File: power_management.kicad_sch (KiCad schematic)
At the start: 34 parts, among them U1 TPS65185

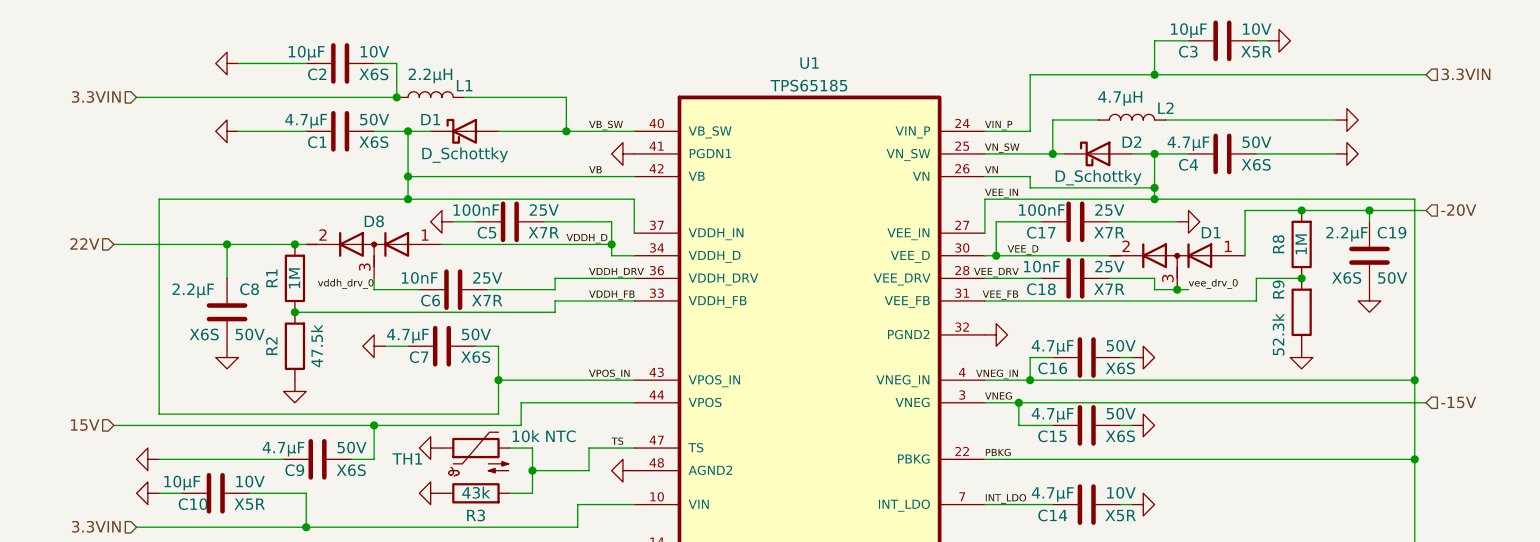
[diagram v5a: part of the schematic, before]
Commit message: Changed VDDH and VEE capacitors to 4.7µF
The evaluation board uses 4.7µF capacitors instead of 2.2µF as stated in
the datasheet.
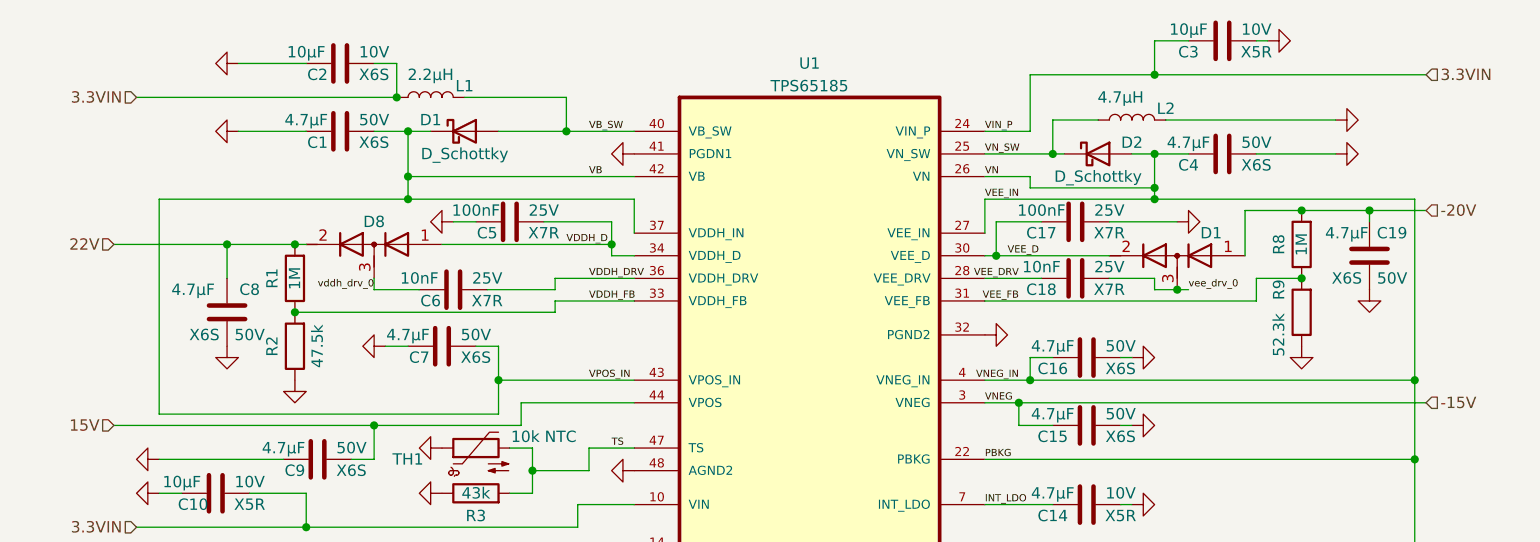
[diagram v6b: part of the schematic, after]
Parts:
- C19, C8: value 2.2µF -> 4.7µF
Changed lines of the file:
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@@
       (effects (font (size 1.27 1.27)))
     )
-    (property "Value" "2.2µF" (at 80.01 67.31 0)
+    (property "Value" "4.7µF" (at 80.01 67.31 0)
       (effects (font (size 1.27 1.27)))
     )
@@
       (effects (font (size 1.27 1.27)))
     )
-    (property "Value" "2.2µF" (at 209.55 60.96 0)
+    (property "Value" "4.7µF" (at 209.55 60.96 0)
       (effects (font (size 1.27 1.27)))
     )

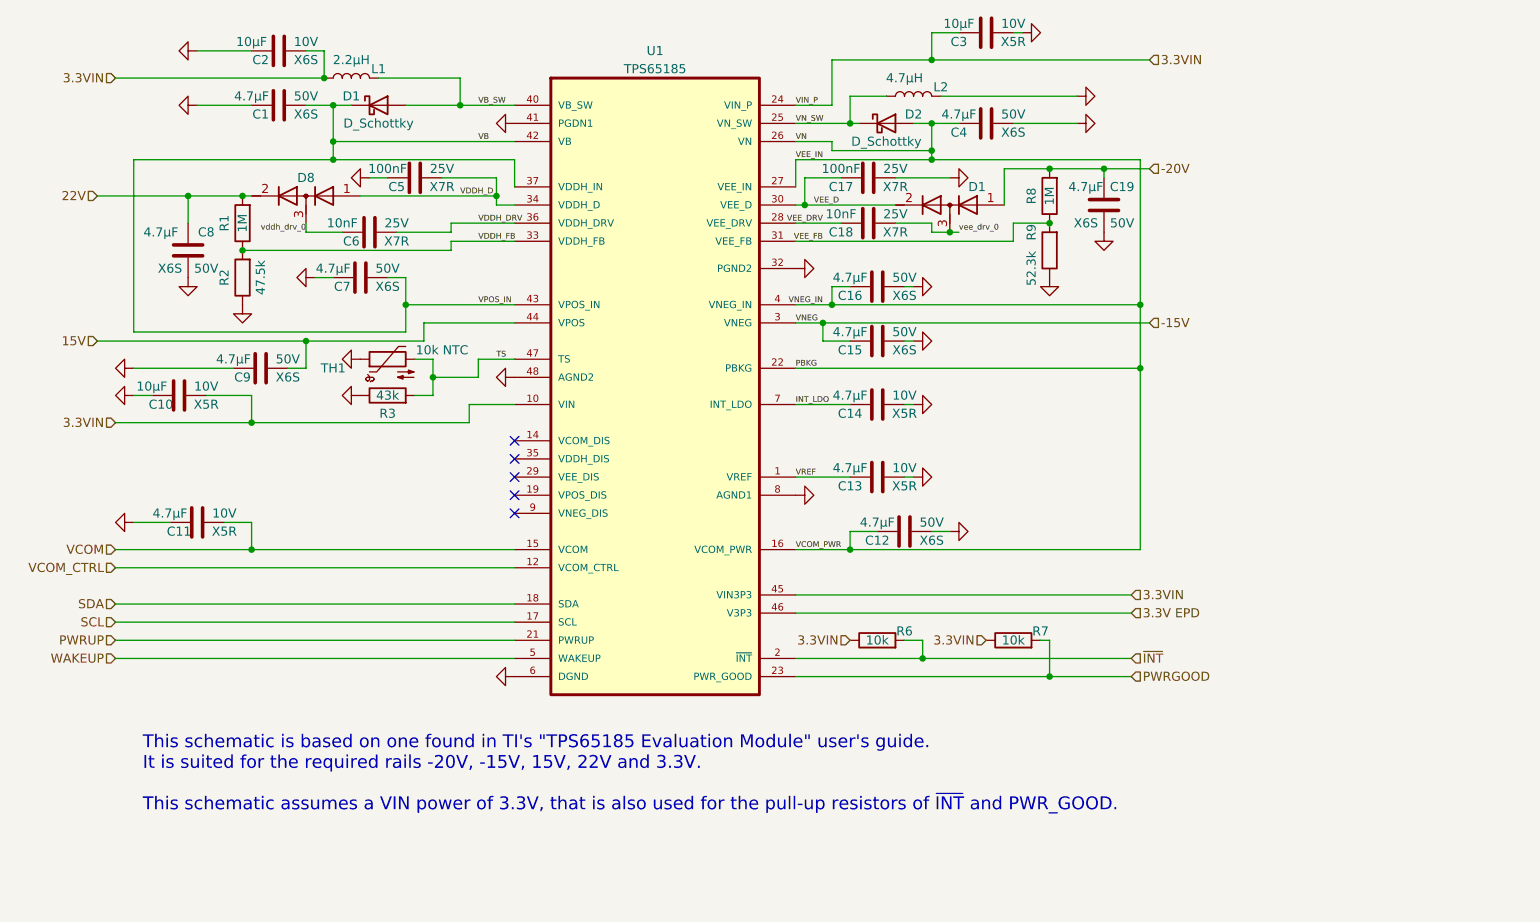
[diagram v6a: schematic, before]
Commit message: Fixed PWR flags in schematic
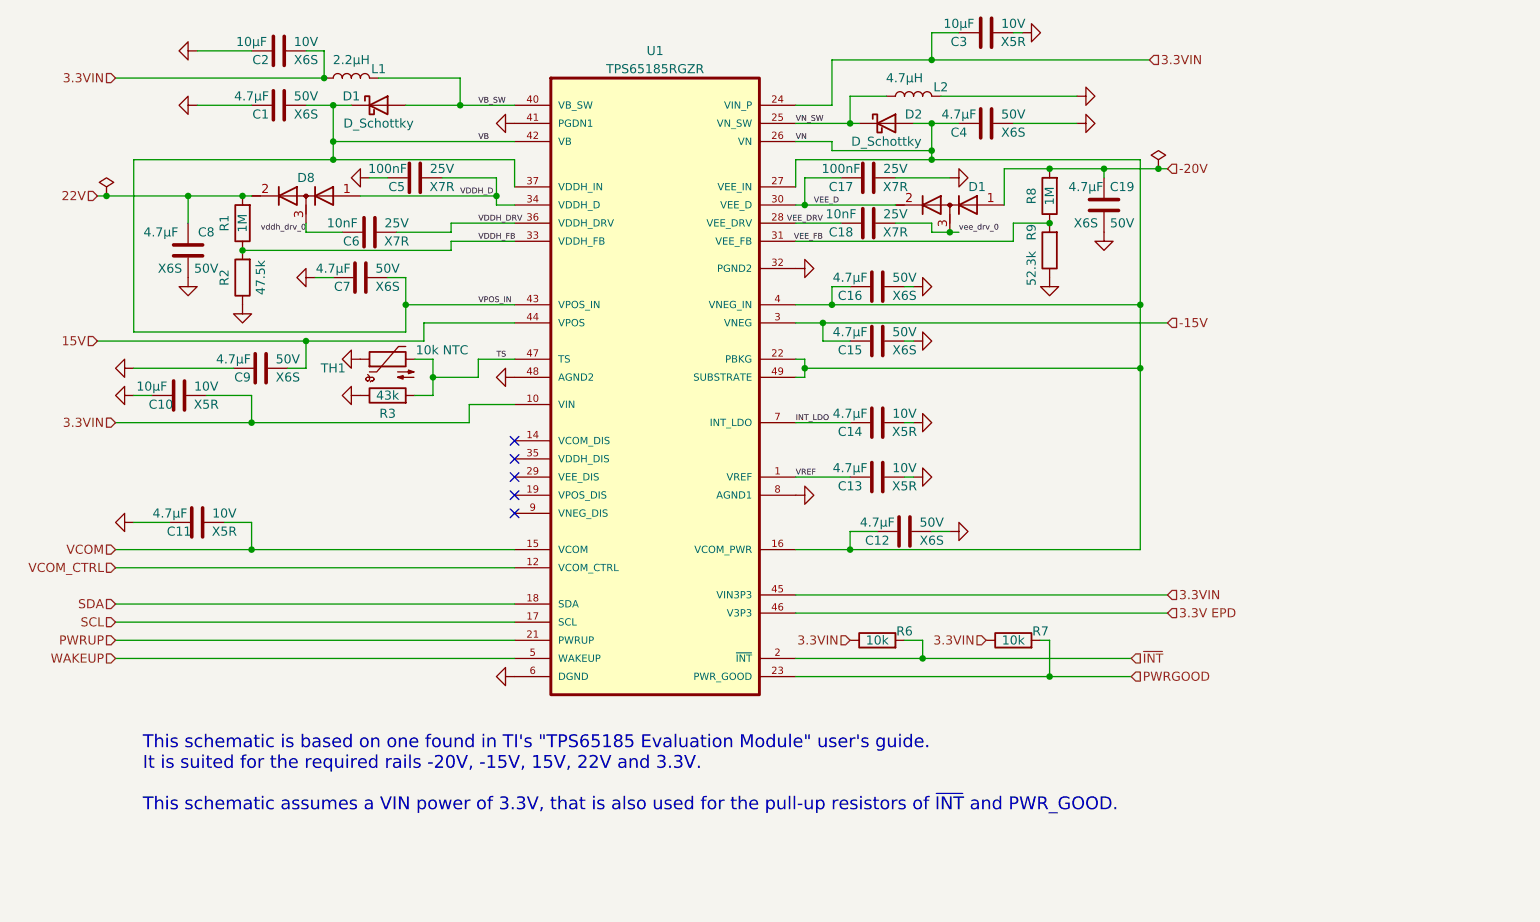
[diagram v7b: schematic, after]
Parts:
- U1: value TPS65185 -> TPS65185RGZR
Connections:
- net PBKG renamed VN
- net VN: now also U1.49 (SUBSTRATE)
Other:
- moved on the sheet: C14

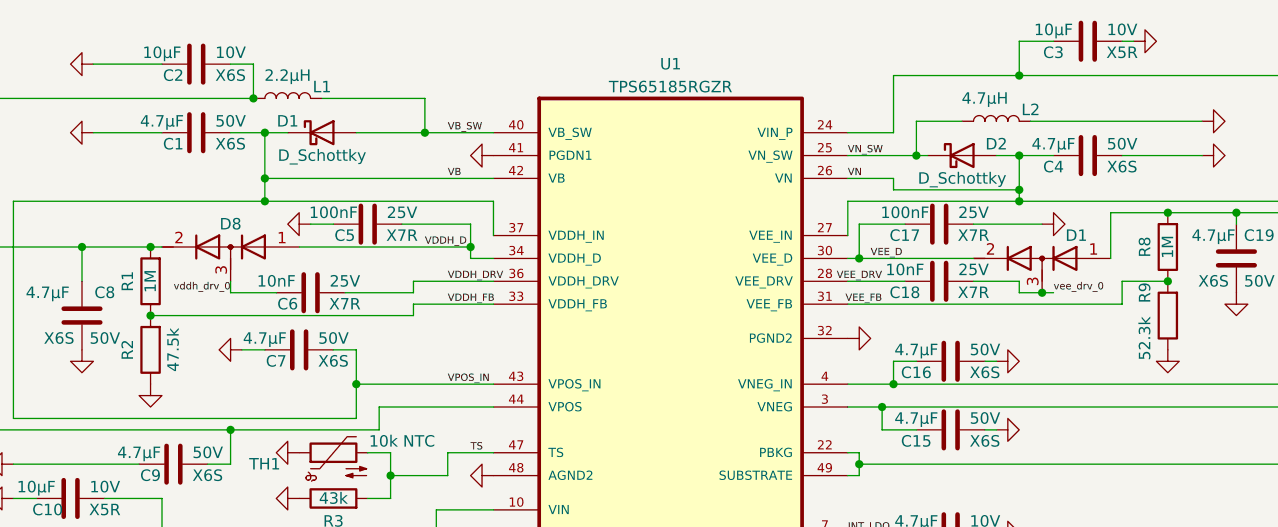
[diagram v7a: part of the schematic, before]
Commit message: Change D footprint for TPS and LCSC part #
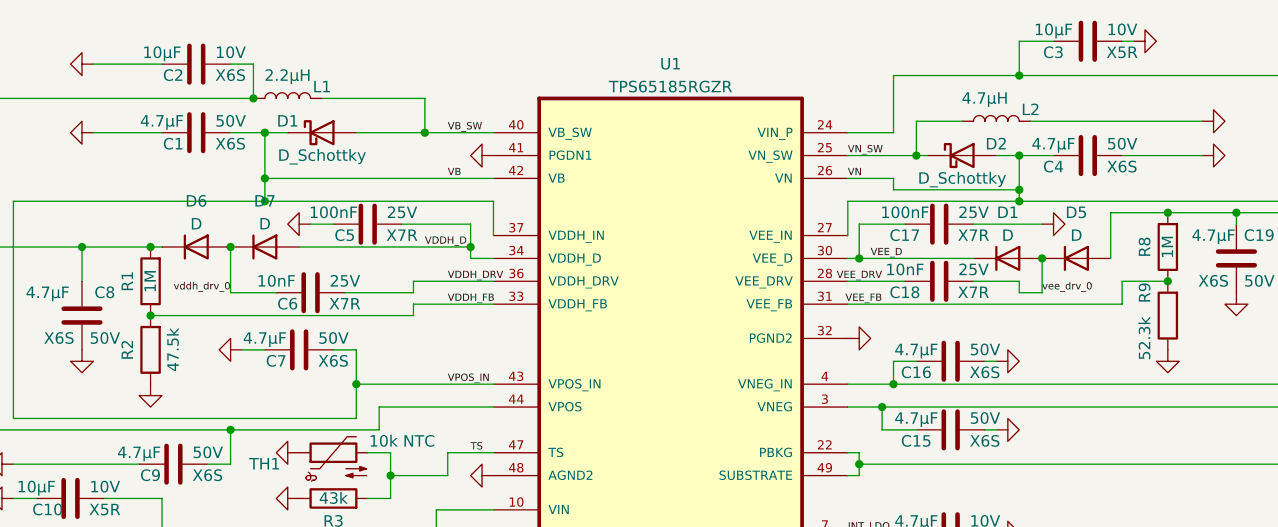
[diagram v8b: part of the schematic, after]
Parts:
- removed D1, D8: D_Dual_Series_AKC, Package_TO_SOT_SMD:SOT-23, symbol Device:D_Dual_Series_AKC
- added D1, D5, D6, D7: D, Diode_SMD:D_SOD-123, symbol Device:D
- C1, C11, C12, C13, C14, C15, C16, C19, C4, C7, C8, C9: LCSC Part # (none) -> C98192
- C10, C2, C3: LCSC Part # (none) -> C85713
- C17, C5: LCSC Part # (none) -> C1591
- C18, C6: LCSC Part # (none) -> C1589
- D1, D2: LCSC Part # (none) -> C82544
- L1: LCSC Part # (none) -> C136232
- L2: LCSC Part # (none) -> C92936
- R1, R8: LCSC Part # (none) -> C105578
- R2: LCSC Part # (none) -> C137715
- R3: LCSC Part # (none) -> C137719
- R6, R7: LCSC Part # (none) -> C98220
- R9: LCSC Part # (none) -> C185323
- TH1: LCSC Part # (none) -> C13564
- U1: LCSC Part # (none) -> C139291
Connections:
- net -20V: now also D5.2 (A)
- net 22V: now also D6.1 (K)
- net VDDH_D: now also D7.2 (A)
- net VEE_D: now also D1.1 (K)
- net vddh_drv_0: now also D6.2 (A), D7.1 (K)
- net vee_drv_0: now also D1.2 (A), D5.1 (K)
